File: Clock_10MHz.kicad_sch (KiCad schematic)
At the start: 8 parts, among them U3 74LV8154, U4 74LS151, X1 ASCO

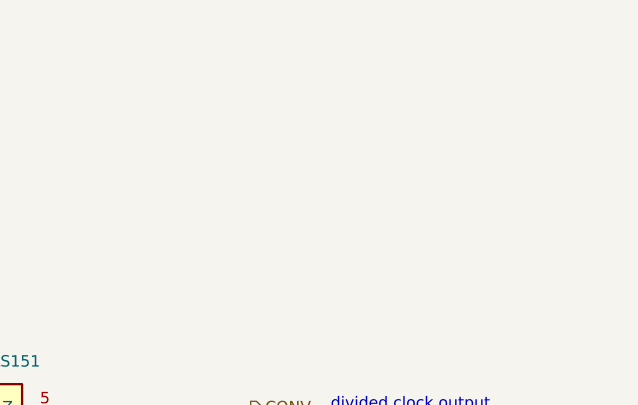
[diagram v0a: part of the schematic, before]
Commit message: added decoupling Cs
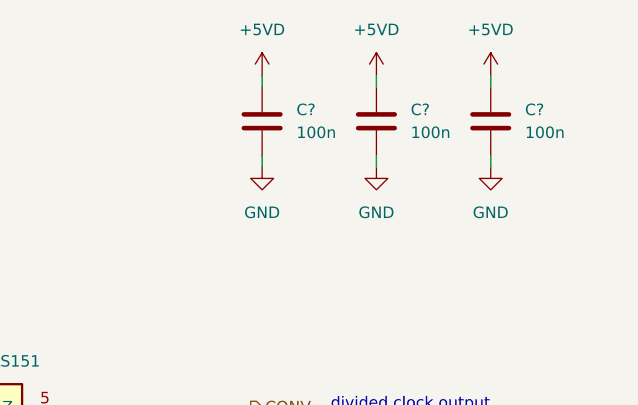
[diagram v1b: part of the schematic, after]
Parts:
- added C? (x3): 100n, Capacitor_SMD:C_0603_1608Metric, symbol Device:C
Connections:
- net +5VD: now also C?.1, C?.1, C?.1
- net GND: now also C?.2, C?.2, C?.2
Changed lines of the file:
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@@
   (junction (at 50.8 90.17) (diameter 0) (color 0 0 0 0)
   )
+  (wire (pts (xy 212.09 44.45) (xy 212.09 45.72))
+    (stroke (width 0) (type default) (color 0 0 0 0))
+  )
   (wire (pts (xy 66.04 64.77) (xy 66.04 77.47))
     (stroke (width 0) (type default) (color 0 0 0 0))
@@
     (stroke (width 0) (type default) (color 0 0 0 0))
   )
+  (wire (pts (xy 224.79 35.56) (xy 224.79 36.83))
+    (stroke (width 0) (type default) (color 0 0 0 0))
+  )
   (wire (pts (xy 146.05 82.55) (xy 152.4 82.55))
     (stroke (width 0) (type default) (color 0 0 0 0))
@@
     (stroke (width 0) (type default) (color 0 0 0 0))
   )
+  (wire (pts (xy 199.39 44.45) (xy 199.39 45.72))
+    (stroke (width 0) (type default) (color 0 0 0 0))
+  )
   (wire (pts (xy 85.09 72.39) (xy 85.09 74.93))
     (stroke (width 0) (type default) (color 0 0 0 0))
@@
     (stroke (width 0) (type default) (color 0 0 0 0))
   )
+  (wire (pts (xy 199.39 35.56) (xy 199.39 36.83))
+    (stroke (width 0) (type default) (color 0 0 0 0))
+  )
   (wire (pts (xy 109.22 82.55) (xy 115.57 82.55))
     (stroke (width 0) (type default) (color 0 0 0 0))
@@
     (stroke (width 0) (type default) (color 0 0 0 0))
   )
+  (wire (pts (xy 212.09 35.56) (xy 212.09 36.83))
+    (stroke (width 0) (type default) (color 0 0 0 0))
+  )
   (wire (pts (xy 78.74 77.47) (xy 88.9 77.47))
     (stroke (width 0) (type default) (color 0 0 0 0))
@@
   )
   (wire (pts (xy 146.05 85.09) (xy 152.4 85.09))
+    (stroke (width 0) (type default) (color 0 0 0 0))
+  )
+  (wire (pts (xy 224.79 44.45) (xy 224.79 45.72))
     (stroke (width 0) (type default) (color 0 0 0 0))
   )
@@
   (hierarchical_label "MUX_SEL_1" (shape input) (at 140.97 97.79 180)
     (effects (font (size 1.27 1.27)) (justify right))
+  )
+  (symbol (lib_id "power:+5VD") (at 212.09 35.56 0) (unit 1)
+    (in_bom yes) (on_board yes) (fields_autoplaced)
+    (property "Reference" "#PWR?" (id 0) (at 212.09 39.37 0)
+      (effects (font (size 1.27 1.27)) hide)
+    )
+    (property "Value" "+5VD" (id 1) (at 212.09 30.48 0))
+    (property "Footprint" "" (id 2) (at 212.09 35.56 0)
+      (effects (font (size 1.27 1.27)) hide)
+    )
+    (property "Datasheet" "" (id 3) (at 212.09 35.56 0)
+      (effects (font (size 1.27 1.27)) hide)
+    )
+    (pin "1")
+  )
+  (symbol (lib_id "Device:C") (at 212.09 40.64 0) (unit 1)
+    (in_bom yes) (on_board yes) (fields_autoplaced)
+    (property "Reference" "C?" (id 0) (at 215.9 39.3699 0)
+      (effects (font (size 1.27 1.27)) (justify left))
+    )
+    (property "Value" "100n" (id 1) (at 215.9 41.9099 0)
+      (effects (font (size 1.27 1.27)) (justify left))
+    )
+    (property "Footprint" "Capacitor_SMD:C_0603_1608Metric" (id 2) (at 213.0552 44.45 0)
+      (effects (font (size 1.27 1.27)) hide)
+    )
+    (property "Datasheet" "~" (id 3) (at 212.09 40.64 0)
+      (effects (font (size 1.27 1.27)) hide)
+    )
+    (pin "1")
+    (pin "2")
+  )
+  (symbol (lib_id "power:GND") (at 224.79 45.72 0) (unit 1)
+    (in_bom yes) (on_board yes) (fields_autoplaced)
+    (property "Reference" "#PWR?" (id 0) (at 224.79 52.07 0)
+      (effects (font (size 1.27 1.27)) hide)
+    )
+    (property "Value" "GND" (id 1) (at 224.79 50.8 0))
+    (property "Footprint" "" (id 2) (at 224.79 45.72 0)
+      (effects (font (size 1.27 1.27)) hide)
+    )
+    (property "Datasheet" "" (id 3) (at 224.79 45.72 0)
+      (effects (font (size 1.27 1.27)) hide)
+    )
+    (pin "1")
   )
   (symbol (lib_id "Device:R") (at 74.8921 82.55 90) (unit 1)
@@
     (pin "2")
   )
+  (symbol (lib_id "power:GND") (at 199.39 45.72 0) (unit 1)
+    (in_bom yes) (on_board yes) (fields_autoplaced)
+    (property "Reference" "#PWR?" (id 0) (at 199.39 52.07 0)
+      (effects (font (size 1.27 1.27)) hide)
+    )
+    (property "Value" "GND" (id 1) (at 199.39 50.8 0))
+    (property "Footprint" "" (id 2) (at 199.39 45.72 0)
+      (effects (font (size 1.27 1.27)) hide)
+    )
+    (property "Datasheet" "" (id 3) (at 199.39 45.72 0)
+      (effects (font (size 1.27 1.27)) hide)
+    )
+    (pin "1")
+  )
   (symbol (lib_id "Device:R") (at 74.93 85.09 90) (unit 1)
     (in_bom yes) (on_board yes)
@@
     (pin "1")
     (pin "2")
+  )
+  (symbol (lib_id "Device:C") (at 224.79 40.64 0) (unit 1)
+    (in_bom yes) (on_board yes) (fields_autoplaced)
+    (property "Reference" "C?" (id 0) (at 228.6 39.3699 0)
+      (effects (font (size 1.27 1.27)) (justify left))
+    )
+    (property "Value" "100n" (id 1) (at 228.6 41.9099 0)
+      (effects (font (size 1.27 1.27)) (justify left))
+    )
+    (property "Footprint" "Capacitor_SMD:C_0603_1608Metric" (id 2) (at 225.7552 44.45 0)
+      (effects (font (size 1.27 1.27)) hide)
+    )
+    (property "Datasheet" "~" (id 3) (at 224.79 40.64 0)
+      (effects (font (size 1.27 1.27)) hide)
+    )
+    (pin "1")
+    (pin "2")
+  )
+  (symbol (lib_id "power:+5VD") (at 224.79 35.56 0) (unit 1)
+    (in_bom yes) (on_board yes) (fields_autoplaced)
+    (property "Reference" "#PWR?" (id 0) (at 224.79 39.37 0)
+      (effects (font (size 1.27 1.27)) hide)
+    )
+    (property "Value" "+5VD" (id 1) (at 224.79 30.48 0))
+    (property "Footprint" "" (id 2) (at 224.79 35.56 0)
+      (effects (font (size 1.27 1.27)) hide)
+    )
+    (property "Datasheet" "" (id 3) (at 224.79 35.56 0)
+      (effects (font (size 1.27 1.27)) hide)
+    )
+    (pin "1")
   )
   (symbol (lib_id "74xx:74LV8154") (at 99.06 85.09 0) (unit 1)
@@
       (effects (font (size 1.27 1.27)) hide)
     )
+    (pin "1")
+  )
+  (symbol (lib_id "power:+5VD") (at 199.39 35.56 0) (unit 1)
+    (in_bom yes) (on_board yes) (fields_autoplaced)
+    (property "Reference" "#PWR?" (id 0) (at 199.39 39.37 0)
+      (effects (font (size 1.27 1.27)) hide)
+    )
+    (property "Value" "+5VD" (id 1) (at 199.39 30.48 0))
+    (property "Footprint" "" (id 2) (at 199.39 35.56 0)
+      (effects (font (size 1.27 1.27)) hide)
+    )
+    (property "Datasheet" "" (id 3) (at 199.39 35.56 0)
+      (effects (font (size 1.27 1.27)) hide)
+    )
+    (pin "1")
+  )
+  (symbol (lib_id "Device:C") (at 199.39 40.64 0) (unit 1)
+    (in_bom yes) (on_board yes) (fields_autoplaced)
+    (property "Reference" "C?" (id 0) (at 203.2 39.3699 0)
+      (effects (font (size 1.27 1.27)) (justify left))
+    )
+    (property "Value" "100n" (id 1) (at 203.2 41.9099 0)
+      (effects (font (size 1.27 1.27)) (justify left))
+    )
+    (property "Footprint" "Capacitor_SMD:C_0603_1608Metric" (id 2) (at 200.3552 44.45 0)
+      (effects (font (size 1.27 1.27)) hide)
+    )
+    (property "Datasheet" "~" (id 3) (at 199.39 40.64 0)
+      (effects (font (size 1.27 1.27)) hide)
+    )
+    (pin "1")
+    (pin "2")
+  )
+  (symbol (lib_id "power:GND") (at 212.09 45.72 0) (unit 1)
+    (in_bom yes) (on_board yes) (fields_autoplaced)
+    (property "Reference" "#PWR?" (id 0) (at 212.09 52.07 0)
+      (effects (font (size 1.27 1.27)) hide)
+    )
+    (property "Value" "GND" (id 1) (at 212.09 50.8 0))
+    (property "Footprint" "" (id 2) (at 212.09 45.72 0)
+      (effects (font (size 1.27 1.27)) hide)
+    )
+    (property "Datasheet" "" (id 3) (at 212.09 45.72 0)
+      (effects (font (size 1.27 1.27)) hide)
+    )

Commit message: changed title block to meaningful information
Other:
- title: (none) -> Open Nano Amp Meter
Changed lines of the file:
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@@
 (kicad_sch (version 20211123) (generator eeschema)
   (paper "A4")
+  (title_block
+    (title "Open Nano Amp Meter")
+    (date "2022-11-17")
+    (rev "0.9")
+  )
   (junction (at 85.09 90.17) (diameter 0) (color 0 0 0 0)
   )

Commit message: enumeration done
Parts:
- gave numbers to parts that had none: 3
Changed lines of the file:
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@@
   (symbol (lib_id "power:+5VD") (at 212.09 35.56 0) (unit 1)
     (in_bom yes) (on_board yes) (fields_autoplaced)
-    (property "Reference" "#PWR?" (id 0) (at 212.09 39.37 0)
+    (property "Reference" "#PWR026" (id 0) (at 212.09 39.37 0)
       (effects (font (size 1.27 1.27)) hide)
     )
@@
   (symbol (lib_id "Device:C") (at 212.09 40.64 0) (unit 1)
     (in_bom yes) (on_board yes) (fields_autoplaced)
-    (property "Reference" "C?" (id 0) (at 215.9 39.3699 0)
+    (property "Reference" "C16" (id 0) (at 215.9 39.3699 0)
       (effects (font (size 1.27 1.27)) (justify left))
     )
@@
   (symbol (lib_id "power:GND") (at 224.79 45.72 0) (unit 1)
     (in_bom yes) (on_board yes) (fields_autoplaced)
-    (property "Reference" "#PWR?" (id 0) (at 224.79 52.07 0)
+    (property "Reference" "#PWR029" (id 0) (at 224.79 52.07 0)
       (effects (font (size 1.27 1.27)) hide)
     )
@@
   (symbol (lib_id "power:GND") (at 199.39 45.72 0) (unit 1)
     (in_bom yes) (on_board yes) (fields_autoplaced)
-    (property "Reference" "#PWR?" (id 0) (at 199.39 52.07 0)
+    (property "Reference" "#PWR025" (id 0) (at 199.39 52.07 0)
       (effects (font (size 1.27 1.27)) hide)
     )
@@
   (symbol (lib_id "Device:C") (at 224.79 40.64 0) (unit 1)
     (in_bom yes) (on_board yes) (fields_autoplaced)
-    (property "Reference" "C?" (id 0) (at 228.6 39.3699 0)
+    (property "Reference" "C17" (id 0) (at 228.6 39.3699 0)
       (effects (font (size 1.27 1.27)) (justify left))
     )
@@
   (symbol (lib_id "power:+5VD") (at 224.79 35.56 0) (unit 1)
     (in_bom yes) (on_board yes) (fields_autoplaced)
-    (property "Reference" "#PWR?" (id 0) (at 224.79 39.37 0)
+    (property "Reference" "#PWR028" (id 0) (at 224.79 39.37 0)
       (effects (font (size 1.27 1.27)) hide)
     )
@@
   (symbol (lib_id "power:+5VD") (at 199.39 35.56 0) (unit 1)
     (in_bom yes) (on_board yes) (fields_autoplaced)
-    (property "Reference" "#PWR?" (id 0) (at 199.39 39.37 0)
+    (property "Reference" "#PWR024" (id 0) (at 199.39 39.37 0)
       (effects (font (size 1.27 1.27)) hide)
     )
@@
   (symbol (lib_id "Device:C") (at 199.39 40.64 0) (unit 1)
     (in_bom yes) (on_board yes) (fields_autoplaced)
-    (property "Reference" "C?" (id 0) (at 203.2 39.3699 0)
+    (property "Reference" "C15" (id 0) (at 203.2 39.3699 0)
       (effects (font (size 1.27 1.27)) (justify left))
     )
@@
   (symbol (lib_id "power:GND") (at 212.09 45.72 0) (unit 1)
     (in_bom yes) (on_board yes) (fields_autoplaced)
-    (property "Reference" "#PWR?" (id 0) (at 212.09 52.07 0)
-      (effects (font (size 1.27 1.27)) hide)
-    )
+    (property "Reference" "#PWR027" (id 0) (at 212.09 52.07 0)
+      (effects (font (size 1.27 1.27)) hide)
+    )
